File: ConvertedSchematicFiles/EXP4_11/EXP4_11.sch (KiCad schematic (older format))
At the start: 19 parts, among them U1 uA741

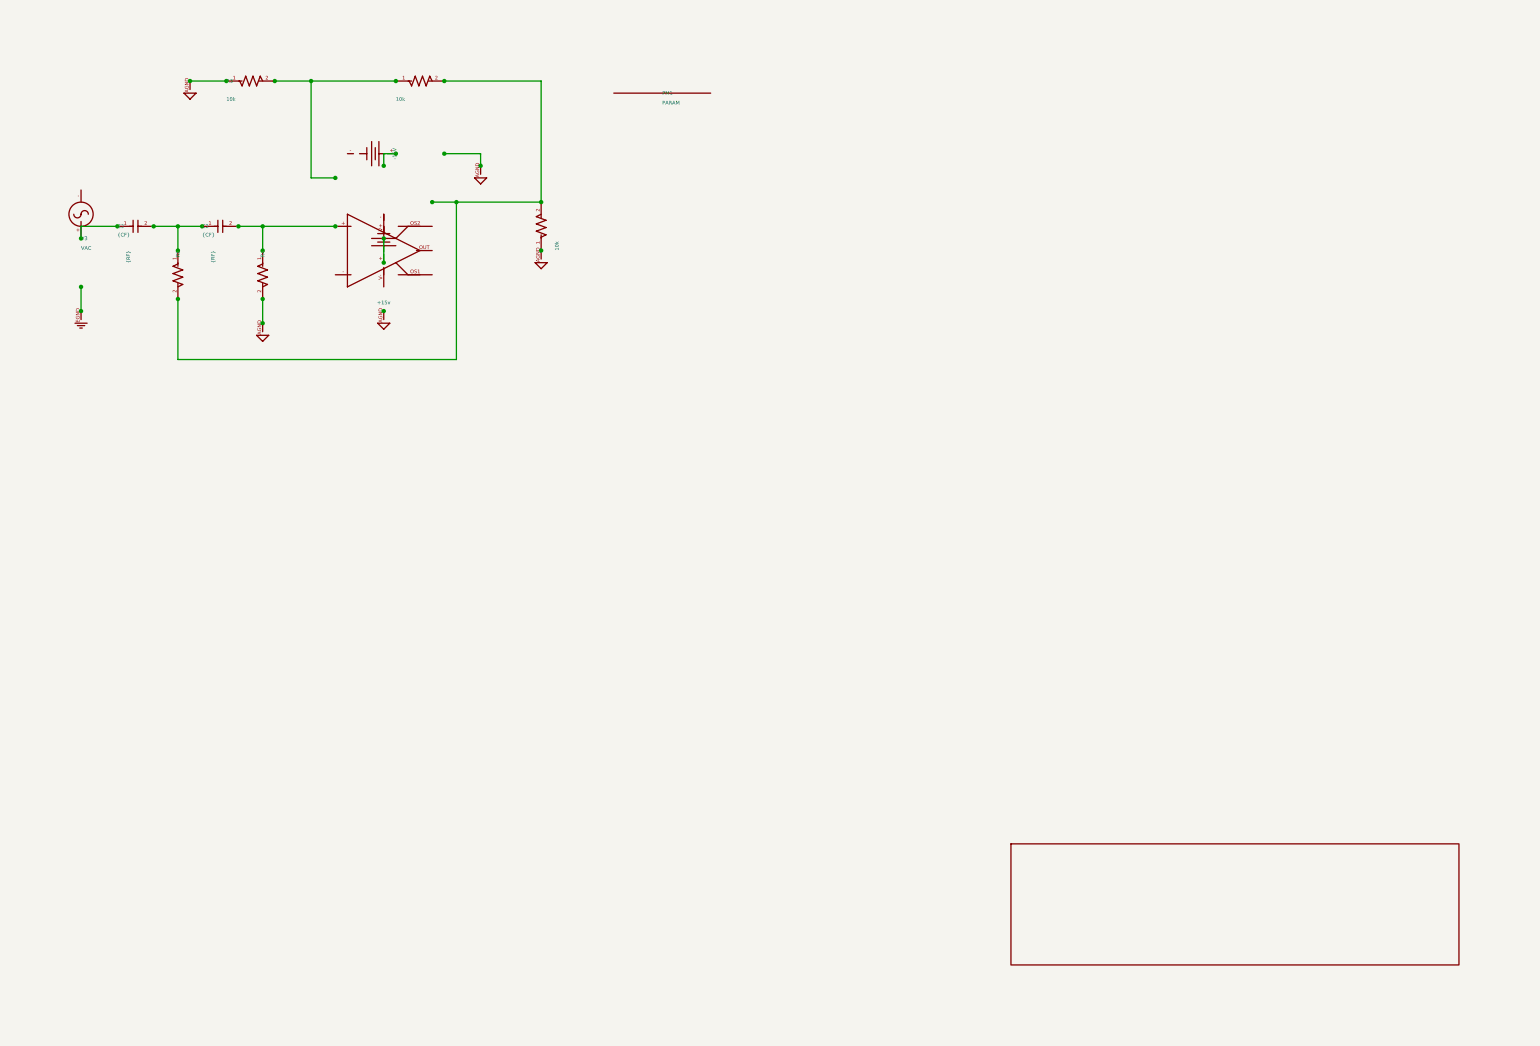
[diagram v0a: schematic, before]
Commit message: Excluded some components. These no longer appear after conversion. When calling shell commands, filenames are in "quotes"
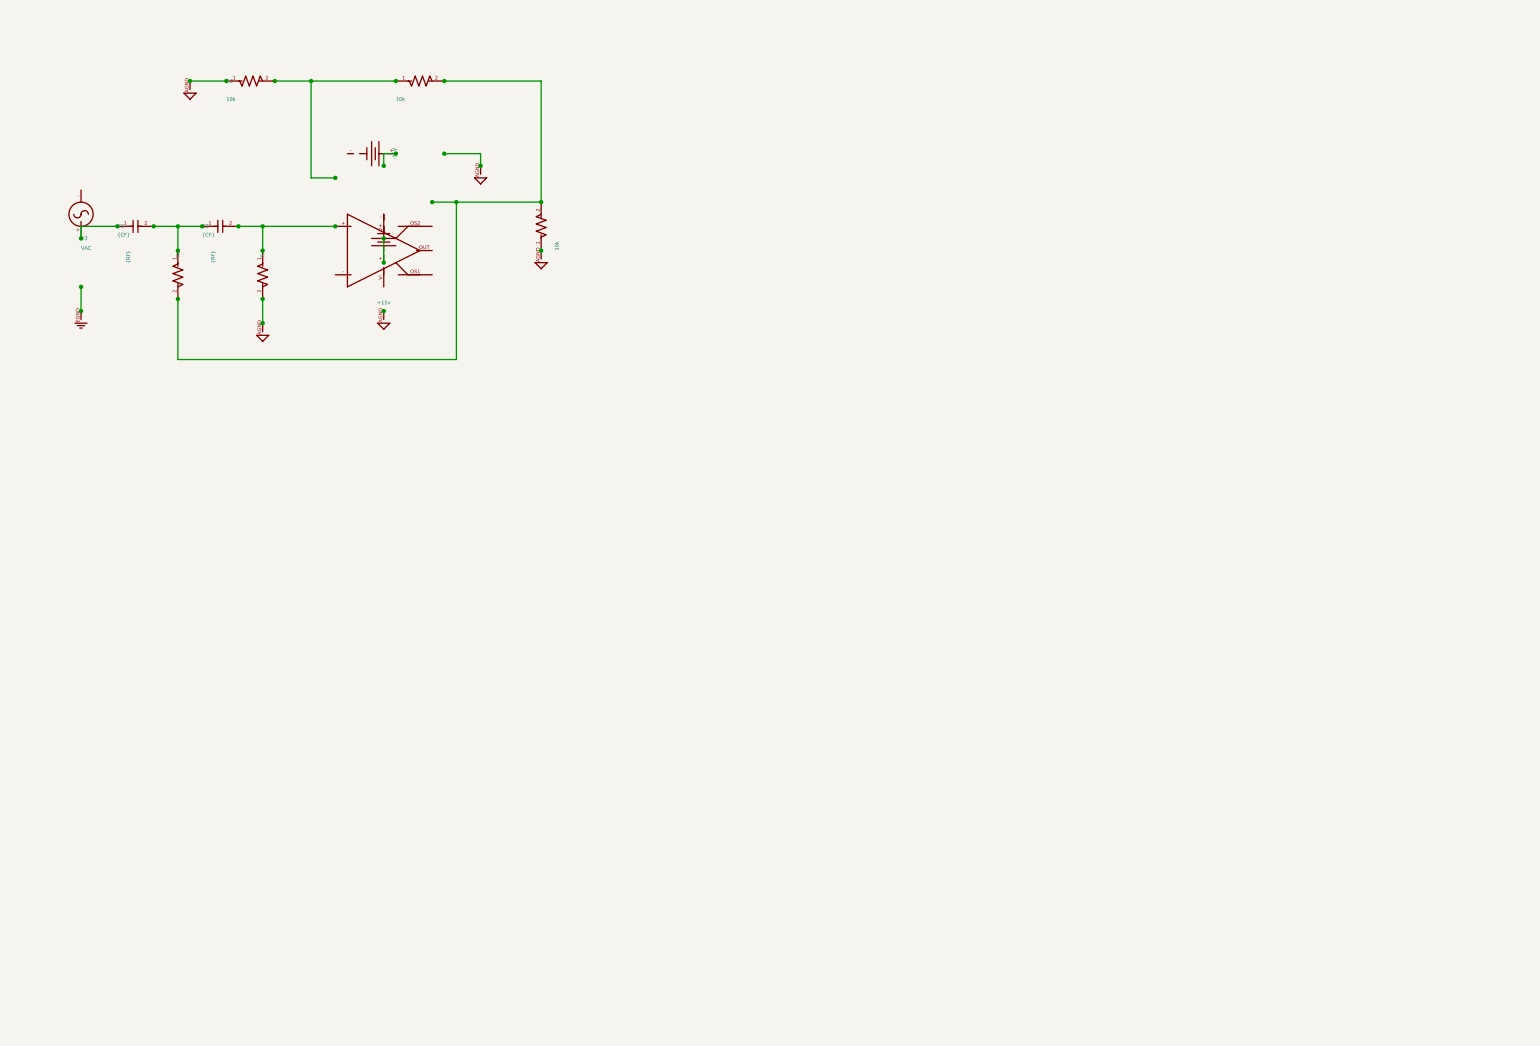
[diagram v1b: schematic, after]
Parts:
- removed PM1: PARAM, symbol PARAM_PSPICE
- removed titleblk: titleblk, symbol TITLEBLK_PSPICE
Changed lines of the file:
@@
 	0    -1    1    0
-$EndComp
-$Comp
-L PARAM_PSPICE PM1
-U 1 1 20383426
-P 5300 1200
-F 0 "PM1" H 5300 1200 30  0000 L CNN
-F 1 "PARAM" H 5300 1280 30  0000 L CNN
-	1    5300 1200
-	1    0    0    1
-$EndComp
-$Comp
-L TITLEBLK_PSPICE titleblk
-U 1 1 44089172
-P 11880 8400
-F 0 "titleblk" H 23760 16800 30  0001 L CNN
-F 1 "titleblk" H 23760 16880 30  0001 L CNN
-	1    11880 8400
-	1    0    0    1
 $EndComp
 Wire Wire Line

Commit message: Ports issue fixed. Now annotation for ports is #PWR? function added "itos"
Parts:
- removed EGND: EGND, symbol EGND_PSPICE
- removed GND_ANALOG (x5): GND_ANALOG, symbol GND_ANALOG_PSPICE
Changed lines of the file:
@@
 $EndDescr
 $Comp
-L GND_ANALOG_PSPICE GND_ANALOG
+L GND_ANALOG_PSPICE #PWR1
 U 1 1 14289383
 P 3800 1800
-F 0 "GND_ANALOG" H 7600 3600 30  0001 L CNN
+F 0 "#PWR1" H 7600 3600 30  0001 L CNN
 F 1 "GND_ANALOG" H 7600 3680 30  0001 L CNN
 	1    3800 1800
@@
 $EndComp
 $Comp
-L GND_ANALOG_PSPICE GND_ANALOG
+L GND_ANALOG_PSPICE #PWR2
 U 1 1 46930886
 P 4300 2500
-F 0 "GND_ANALOG" H 8600 5000 30  0001 L CNN
+F 0 "#PWR2" H 8600 5000 30  0001 L CNN
 F 1 "GND_ANALOG" H 8600 5080 30  0001 L CNN
 	1    4300 2500
@@
 $EndComp
 $Comp
-L GND_ANALOG_PSPICE GND_ANALOG
+L GND_ANALOG_PSPICE #PWR3
 U 1 1 71692777
 P 3000 3000
-F 0 "GND_ANALOG" H 6000 6000 30  0001 L CNN
+F 0 "#PWR3" H 6000 6000 30  0001 L CNN
 F 1 "GND_ANALOG" H 6000 6080 30  0001 L CNN
 	1    3000 3000
@@
 $EndComp
 $Comp
-L GND_ANALOG_PSPICE GND_ANALOG
+L GND_ANALOG_PSPICE #PWR4
 U 1 1 14636915
 P 1400 1100
-F 0 "GND_ANALOG" H 2800 2200 30  0001 L CNN
+F 0 "#PWR4" H 2800 2200 30  0001 L CNN
 F 1 "GND_ANALOG" H 2800 2280 30  0001 L CNN
 	1    1400 1100
@@
 $EndComp
 $Comp
-L GND_ANALOG_PSPICE GND_ANALOG
+L GND_ANALOG_PSPICE #PWR5
 U 1 1 77747793
 P 2000 3100
-F 0 "GND_ANALOG" H 4000 6200 30  0001 L CNN
+F 0 "#PWR5" H 4000 6200 30  0001 L CNN
 F 1 "GND_ANALOG" H 4000 6280 30  0001 L CNN
 	1    2000 3100
@@
 $EndComp
 $Comp
-L EGND_PSPICE EGND
+L EGND_PSPICE #PWR6
 U 1 1 74238335
 P 500 3000
-F 0 "EGND" H 1000 6000 30  0001 L CNN
+F 0 "#PWR6" H 1000 6000 30  0001 L CNN
 F 1 "EGND" H 1000 6080 30  0001 L CNN
 	1    500 3000

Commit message: Added LICENSE.txt
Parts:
- V3: value VAC -> AC
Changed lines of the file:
@@
 $EndDescr
 $Comp
-L GND_ANALOG_PSPICE #PWR1
+L AGND #PWR1
 U 1 1 14289383
 P 3800 1800
@@
 $EndComp
 $Comp
-L GND_ANALOG_PSPICE #PWR2
+L AGND #PWR2
 U 1 1 46930886
 P 4300 2500
@@
 $EndComp
 $Comp
-L GND_ANALOG_PSPICE #PWR3
+L AGND #PWR3
 U 1 1 71692777
 P 3000 3000
@@
 $EndComp
 $Comp
-L GND_ANALOG_PSPICE #PWR4
+L AGND #PWR4
 U 1 1 14636915
 P 1400 1100
@@
 $EndComp
 $Comp
-L GND_ANALOG_PSPICE #PWR5
+L AGND #PWR5
 U 1 1 77747793
 P 2000 3100
@@
 $EndComp
 $Comp
-L EGND_PSPICE #PWR6
+L GND #PWR6
 U 1 1 74238335
 P 500 3000
@@
 P 500 2400
 F 0 "V3" H 500 2400 30  0000 L CNN
-F 1 "VAC" H 500 2480 30  0000 L CNN
+F 1 "AC" H 500 2480 30  0000 L CNN
 	1    500 2400
 	1    0    0    1

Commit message: Orientation fix. Library components are now inverted, with +ve y axis going up. In Schematic files, +ve y axis is downwards. This is how the KiCad libraries are. As a result of the above fixed, the converted GND is now oriented correctly.
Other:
- moved on the sheet: V3
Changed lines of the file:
@@
 F 1 "GND_ANALOG" H 7600 3680 30  0001 L CNN
 	1    3800 1800
-	1    0    0    1
+	1    0    0    -1
 $EndComp
 $Comp
@@
 F 1 "GND_ANALOG" H 8600 5080 30  0001 L CNN
 	1    4300 2500
-	1    0    0    1
+	1    0    0    -1
 $EndComp
 $Comp
@@
 F 1 "GND_ANALOG" H 6000 6080 30  0001 L CNN
 	1    3000 3000
-	1    0    0    1
+	1    0    0    -1
 $EndComp
 $Comp
@@
 F 1 "GND_ANALOG" H 2800 2280 30  0001 L CNN
 	1    1400 1100
-	1    0    0    1
+	1    0    0    -1
 $EndComp
 $Comp
@@
 F 1 "GND_ANALOG" H 4000 6280 30  0001 L CNN
 	1    2000 3100
-	1    0    0    1
+	1    0    0    -1
 $EndComp
 $Comp
@@
 F 1 "EGND" H 1000 6080 30  0001 L CNN
 	1    500 3000
-	1    0    0    1
+	1    0    0    -1
 $EndComp
 $Comp
@@
 F 1 "-15V" H 3100 1690 30  0000 C CNN
 	1    3100 1700
-	0    1    -1    0
+	0    -1    -1    0
 $EndComp
 $Comp
@@
 F 1 "10k" H 3100 1250 30  0000 L CNN
 	1    3100 1100
-	1    0    0    1
+	1    0    0    -1
 $EndComp
 $Comp
@@
 F 1 "10k" H 1700 1250 30  0000 L CNN
 	1    1700 1100
-	1    0    0    1
+	1    0    0    -1
 $EndComp
 $Comp
@@
 F 1 "10k" H 4300 2630 30  0000 L CNN
 	1    4300 2500
-	0    1    -1    0
+	0    -1    -1    0
 $EndComp
 $Comp
@@
 F 1 "{RF}" H 2000 2910 30  0000 L CNN
 	1    2000 2500
-	0    -1    1    0
+	0    1    1    0
 $EndComp
 $Comp
@@
 F 1 "uA741" H 2600 2380 30  0001 L CNN
 	1    2600 2300
-	1    0    0    -1
+	1    0    0    1
 $EndComp
 $Comp
@@
 F 1 "+15v" H 3000 2930 30  0000 C CNN
 	1    3000 2600
-	1    0    0    1
+	1    0    0    -1
 $EndComp
 $Comp
@@
 F 1 "{CF}" H 800 2370 30  0000 L CNN
 	1    800 2300
-	1    0    0    1
+	1    0    0    -1
 $EndComp
 $Comp
@@
 F 1 "AC" H 500 2480 30  0000 L CNN
 	1    500 2400
-	1    0    0    1
+	1    0    0    -1
 $EndComp
 $Comp
@@
 F 1 "{CF}" H 1500 2370 30  0000 L CNN
 	1    1500 2300
-	1    0    0    1
+	1    0    0    -1
 $EndComp
 $Comp
@@
 F 1 "{RF}" H 1300 2910 30  0000 L CNN
 	1    1300 2500
-	0    -1    1    0
+	0    1    1    0
 $EndComp
 Wire Wire Line

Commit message: Removed the use of exec, wrote basename function, made integration with eSim easier.
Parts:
- added PM1: PARAM, symbol PARAM_PSPICE
- added titleblk: titleblk, symbol titleblk_PSPICE
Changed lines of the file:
@@
-EESchema Schematic File Version 2  date Wednesday 23 June 1999 08:12:36 PM IST
+EESchema Schematic File Version 2  date
 LIBS:power
 LIBS:device
@@
 LIBS:contrib
 LIBS:valves
-LIBS:ConvertedSchematicFiles/EXP4_11-cache
 EELAYER 25  0
 EELAYER END
@@
 Sheet 1 1
 Title ""
-Date "23 Jun 1999"
+Date ""
 Rev ""
 Comp ""
@@
 	0    1    1    0
 $EndComp
+$Comp
+L PARAM_PSPICE PM1
+U 1 1 20383426
+P 5300 1200
+F 0 "PM1" H 5300 1200 30  0000 L CNN
+F 1 "PARAM" H 5300 1280 30  0000 L CNN
+	1    5300 1200
+	1    0    0    -1
+$EndComp
+$Comp
+L titleblk_PSPICE titleblk
+U 1 1 44089172
+P 11880 8400
+F 0 "titleblk" H 23760 16800 30  0001 L CNN
+F 1 "titleblk" H 23760 16880 30  0001 L CNN
+	1    11880 8400
+	1    0    0    -1
+$EndComp
 Wire Wire Line
